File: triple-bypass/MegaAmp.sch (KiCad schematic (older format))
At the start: 55 parts, among them U1 LMV358M8G-13

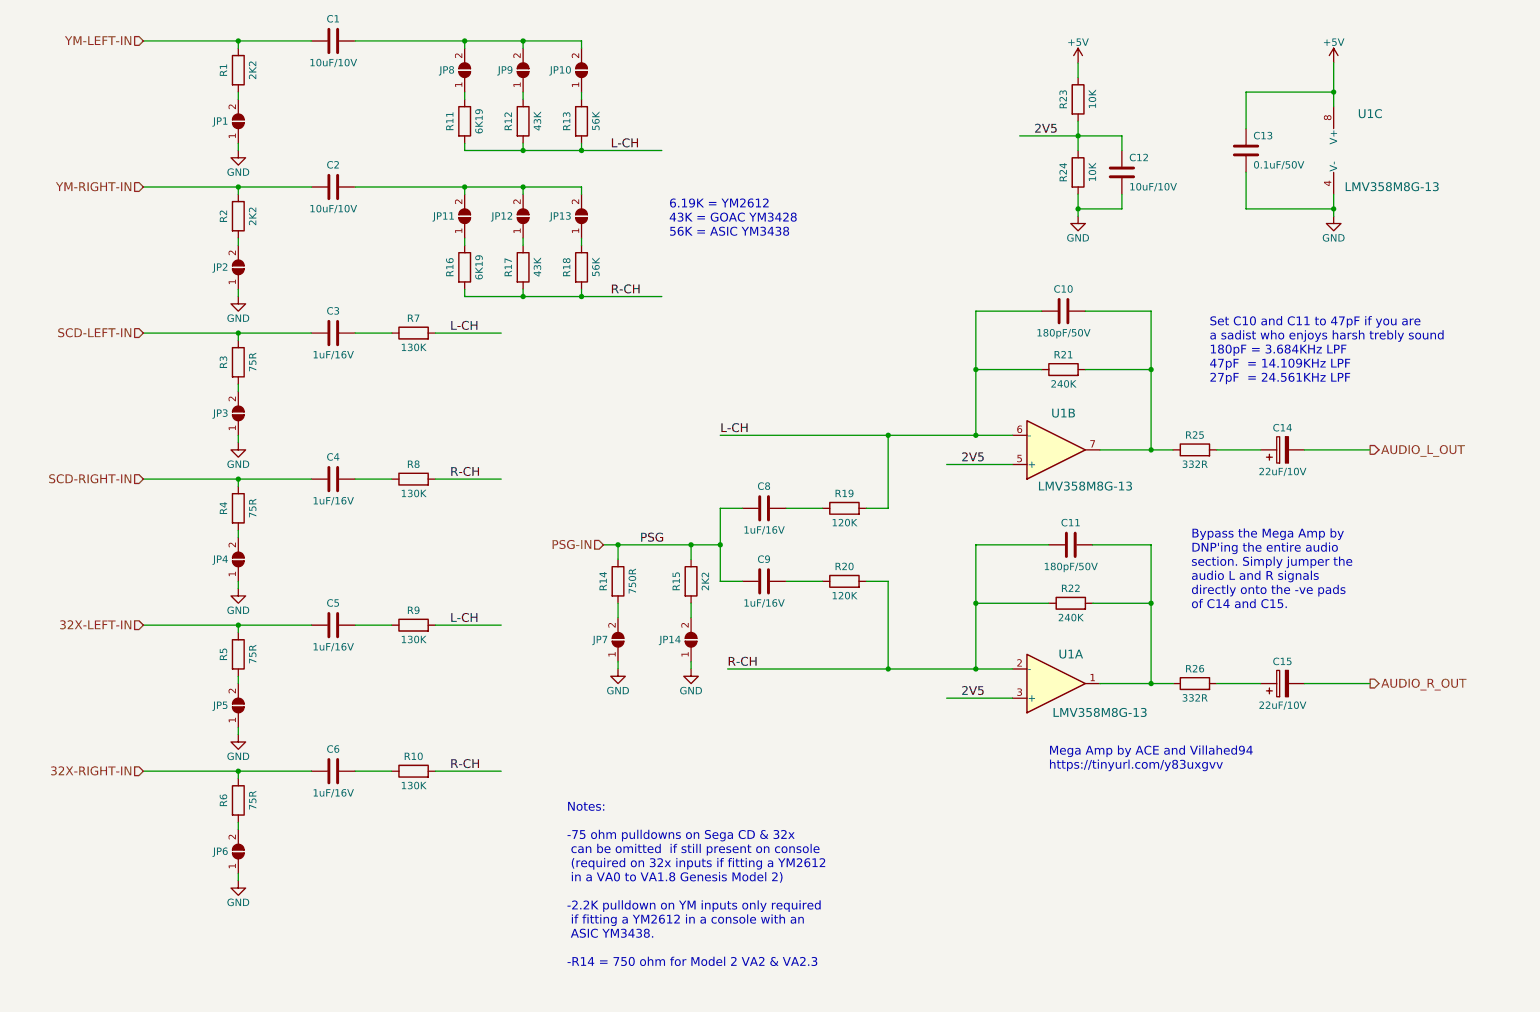
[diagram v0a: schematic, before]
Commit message: Rename to AIO
Moved offset of PCB so footprints are on grid. Saved in KiCad version 5.1.0. Export gerbers. Found and deleted board cuts in MiniDIN footprint.
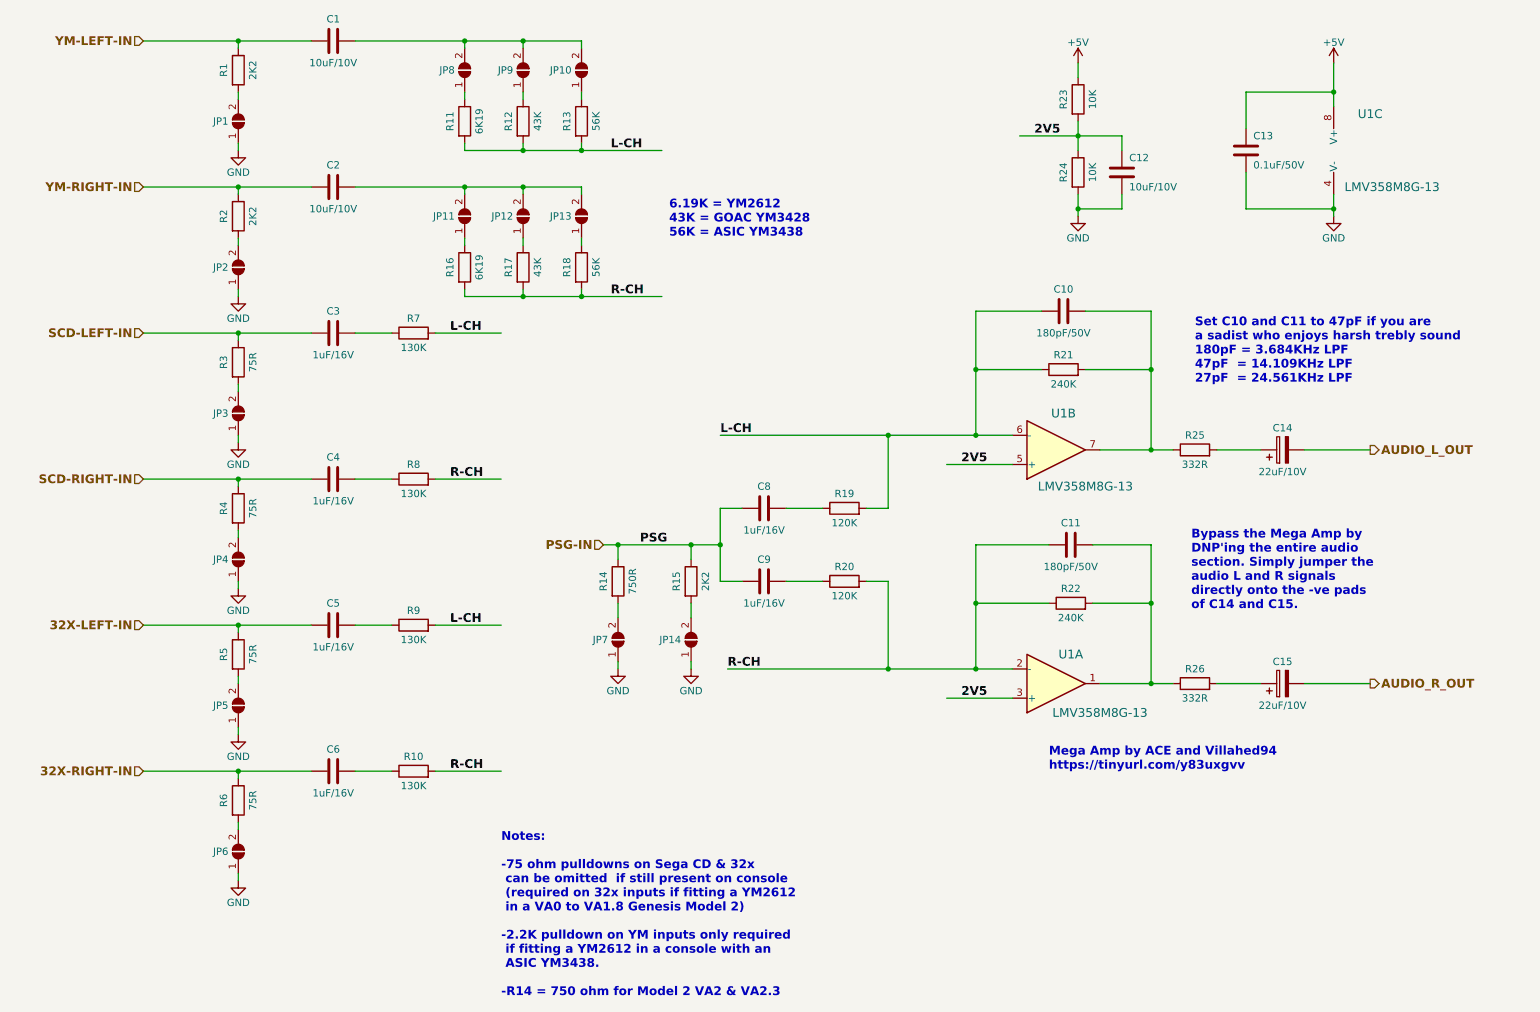
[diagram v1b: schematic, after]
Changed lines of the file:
@@
 EESchema Schematic File Version 4
-LIBS:triple-bypass-cache
-EELAYER 26 0
+LIBS:triple-bypass-aio-cache
+EELAYER 29 0
 EELAYER END
 $Descr A 11000 8500
 encoding utf-8
 Sheet 2 3
-Title "Triple Bypass"
-Date "2018-12-16"
+Title "Triple Bypass AIO"
+Date "2019-03-23"
 Rev "0.4"
 Comp ""
@@
 	1    0    0    -1
 $EndComp
-Text Notes 7500 5950 0    60   ~ 0
+Text Notes 7500 5950 0    60   ~ 12
 Mega Amp by ACE and Villahed94\nhttps://tinyurl.com/y83uxgvv
-Text Label 4700 4400 0    60   ~ 0
+Text Label 4700 4400 0    60   ~ 12
 PSG
-Text Notes 8600 3300 0    60   ~ 0
+Text Notes 8500 3300 0    60   ~ 12
 Set C10 and C11 to 47pF if you are \na sadist who enjoys harsh trebly sound\n180pF = 3.684KHz LPF\n47pF  = 14.109KHz LPF\n27pF  = 24.561KHz LPF
-Text Notes 8475 4850 0    60   ~ 0
+Text Notes 8475 4850 0    60   ~ 12
 Bypass the Mega Amp by \nDNP'ing the entire audio \nsection. Simply jumper the\naudio L and R signals \ndirectly onto the -ve pads \nof C14 and C15.
-Text Notes 4200 7300 0    60   ~ 0
+Text Notes 3750 7500 0    60   ~ 12
 Notes:\n\n-75 ohm pulldowns on Sega CD & 32x \n can be omitted  if still present on console\n (required on 32x inputs if fitting a YM2612 \n in a VA0 to VA1.8 Genesis Model 2)\n\n-2.2K pulldown on YM inputs only required\n if fitting a YM2612 in a console with an \n ASIC YM3438.\n\n-R14 = 750 ohm for Model 2 VA2 & VA2.3
 Wire Wire Line
@@
 Wire Wire Line
 	7700 1600 7300 1600
-Text Label 7400 1600 0    60   ~ 0
+Text Label 7400 1600 0    60   ~ 12
 2V5
-Text Label 6900 5450 0    60   ~ 0
+Text Label 6900 5450 0    60   ~ 12
 2V5
-Text Label 6900 3850 0    60   ~ 0
+Text Label 6900 3850 0    60   ~ 12
 2V5
-Text HLabel 9700 5350 2    60   Output ~ 0
+Text HLabel 9700 5350 2    60   Output ~ 12
 AUDIO_R_OUT
-Text HLabel 9700 3750 2    60   Output ~ 0
+Text HLabel 9700 3750 2    60   Output ~ 12
 AUDIO_L_OUT
 Wire Wire Line
@@
 Wire Wire Line
 	9250 5350 9700 5350
-Text HLabel 1300 950  0    60   Input ~ 0
+Text HLabel 1300 950  0    60   Input ~ 12
 YM-LEFT-IN
-Text HLabel 1300 2950 0    60   Input ~ 0
+Text HLabel 1300 2950 0    60   Input ~ 12
 SCD-LEFT-IN
-Text HLabel 1300 4950 0    60   Input ~ 0
+Text HLabel 1300 4950 0    60   Input ~ 12
 32X-LEFT-IN
-Text HLabel 4450 4400 0    60   Input ~ 0
+Text HLabel 4450 4400 0    60   Input ~ 12
 PSG-IN
-Text HLabel 1300 5950 0    60   Input ~ 0
+Text HLabel 1300 5950 0    60   Input ~ 12
 32X-RIGHT-IN
-Text HLabel 1300 3950 0    60   Input ~ 0
+Text HLabel 1300 3950 0    60   Input ~ 12
 SCD-RIGHT-IN
 Wire Wire Line
@@
 	0    1    1    0
 $EndComp
-Text HLabel 1300 1950 0    60   Input ~ 0
+Text HLabel 1300 1950 0    60   Input ~ 12
 YM-RIGHT-IN
 Connection ~ 6400 3650
@@
 Wire Wire Line
 	5250 3650 6400 3650
-Text Label 3400 2950 0    60   ~ 0
+Text Label 3400 2950 0    60   ~ 12
 L-CH
-Text Label 3400 4950 0    60   ~ 0
+Text Label 3400 4950 0    60   ~ 12
 L-CH
 Wire Wire Line
@@
 Wire Wire Line
 	3300 2950 3750 2950
-Text Label 4500 1700 0    60   ~ 0
+Text Label 4500 1700 0    60   ~ 12
 L-CH
-Text Label 3400 3950 0    60   ~ 0
+Text Label 3400 3950 0    60   ~ 12
 R-CH
-Text Label 3400 5950 0    60   ~ 0
+Text Label 3400 5950 0    60   ~ 12
 R-CH
-Text Label 5250 3650 0    60   ~ 0
+Text Label 5250 3650 0    60   ~ 12
 L-CH
-Text Label 5300 5250 0    60   ~ 0
+Text Label 5300 5250 0    60   ~ 12
 R-CH
-Text Notes 4900 2300 0    60   ~ 0
+Text Notes 4900 2300 0    60   ~ 12
 6.19K = YM2612\n43K = GOAC YM3428\n56K = ASIC YM3438
 $Comp
@@
 	3500 1950 2750 1950
 Connection ~ 3500 1950
-Text Label 4500 2700 0    60   ~ 0
+Text Label 4500 2700 0    60   ~ 12
 R-CH
 Wire Wire Line
